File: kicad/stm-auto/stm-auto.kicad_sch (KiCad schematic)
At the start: 18 parts, among them M1 Motor_Servo, M2 Motor_Servo, U2 PSSMOPS, U3 SN65HVD230, U4 STM32F103C8Tx

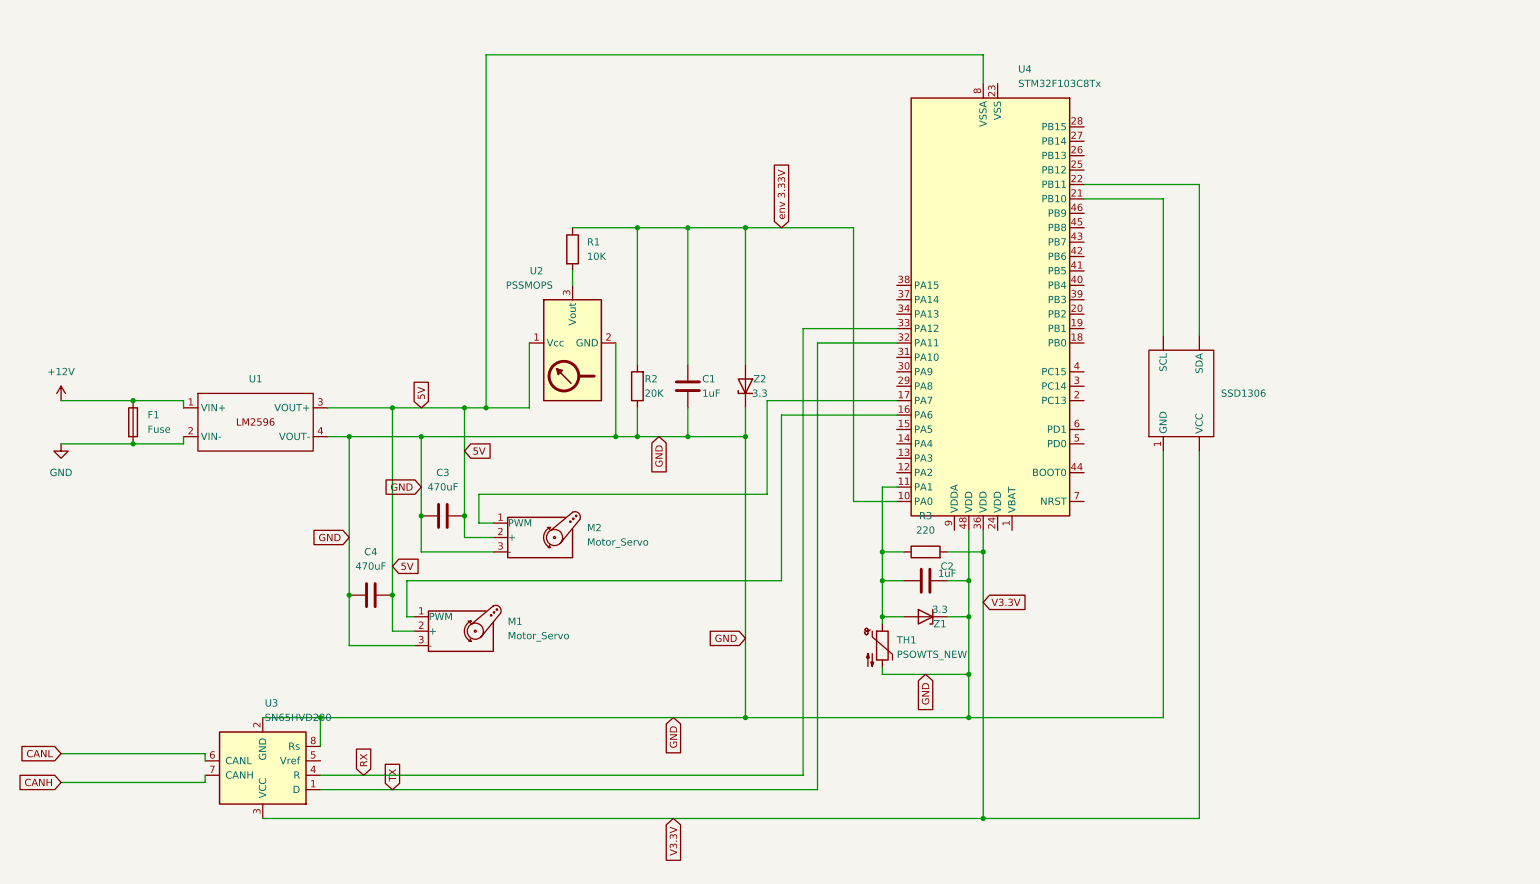
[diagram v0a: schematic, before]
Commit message: #8 docs: add peripheral wiring decisions and refresh schematic
Add kicad/stm-auto/WIRING.md capturing the locked wiring choices for the
WS2812B (diode drop to ~4.3V), buzzer (passive piezo, direct drive), ACK
touch button (3.3V, PB5 input) and DFPlayer MP3 (5V, SPK speaker). Update
the schematic and regenerate the SVG. Gitignore the per-user .kicad_prl.

Co-Authored-By: Claude Opus 4.8 <noreply@anthropic.com>
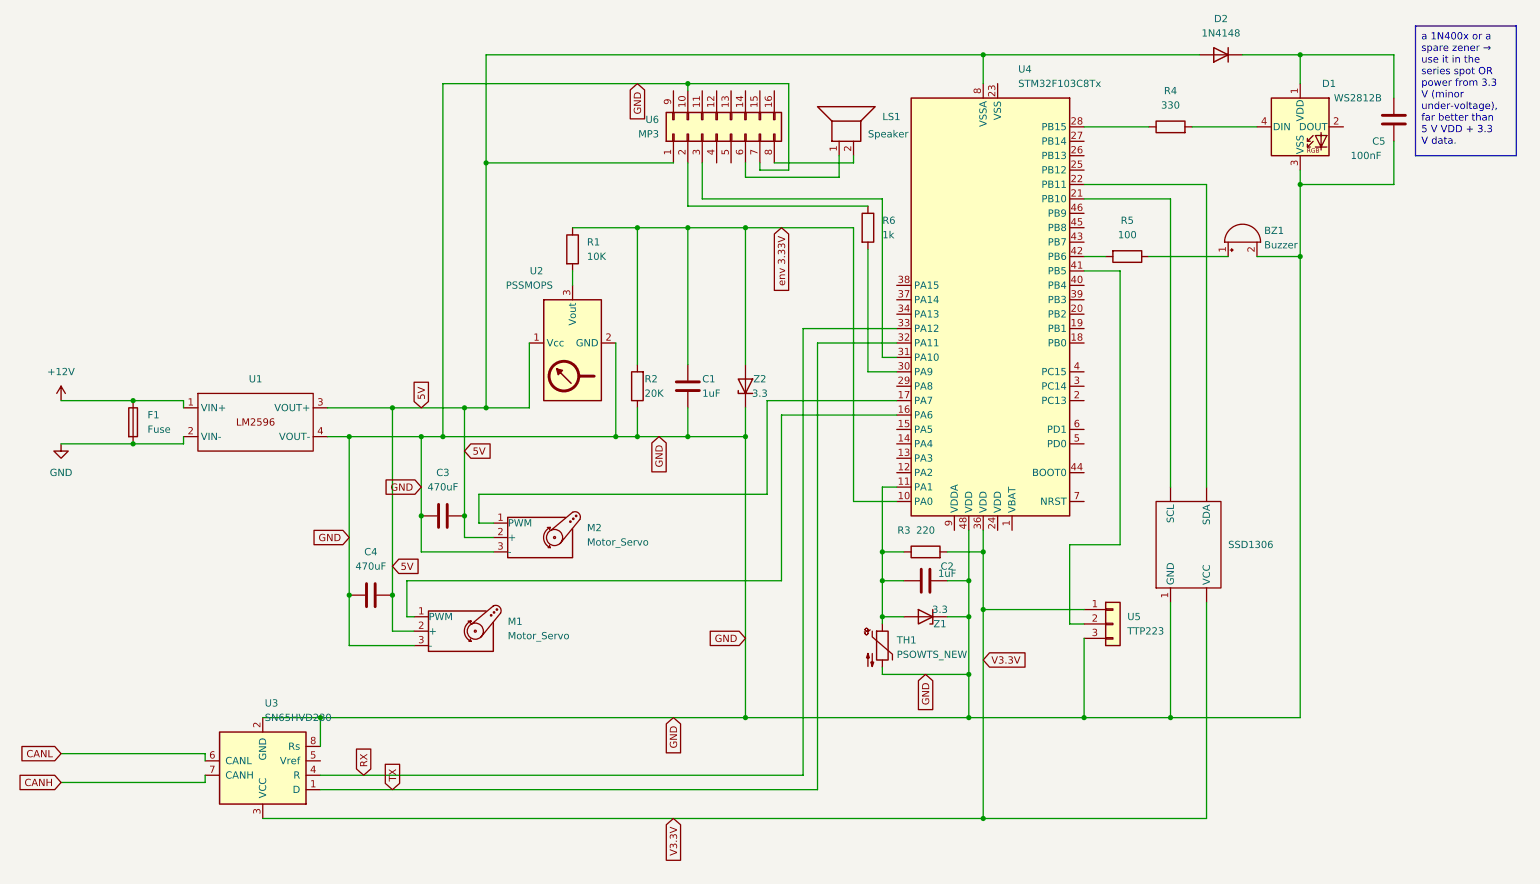
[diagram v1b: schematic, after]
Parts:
- added BZ1: Buzzer, symbol Device:Buzzer
- added C5: 100nF, symbol Device:C
- added D1: WS2812B, LED_SMD:LED_WS2812B_PLCC4_5.0x5.0mm_P3.2mm, symbol LED:WS2812B
- added D2: 1N4148, symbol Device:D
- added LS1: Speaker, symbol Device:Speaker
- added R4: 330, symbol Device:R
- added R5: 100, symbol Device:R
- added R6: 1k, symbol Device:R
- added U5: TTP223, symbol Connector_Generic:Conn_01x03
- added U6: MP3, symbol Connector_Generic:Conn_02x08_Top_Bottom
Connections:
- net 5V: now also D2.2 (A), U6.1 (Pin_1)
- net GND: now also BZ1.2 (-), C5.2, D1.3 (VSS), U5.3 (GND), U6.10 (Pin_10), U6.7 (Pin_7)
- net V3.3V: now also U5.1 (VCC)
- net at U4.28 (PB15): now also R4.1
- net at U4.30 (PA9): now also R6.2
- net at U4.31 (PA10): now also U6.3 (Pin_3)
- net at U4.41 (PB5): now also U5.2 (OUT)
- net at U4.42 (PB6): now also R5.2
- new net: R6.1, U6.2 (Pin_2)
- new net: BZ1.1 (+), R5.1
- new net: C5.1, D1.1 (VDD), D2.1 (K)
- new net: D1.4 (DIN), R4.2
- new net: LS1.1, U6.6 (Pin_6)
- new net: LS1.2, U6.8 (Pin_8)
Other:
- moved on the sheet: SSD1306
